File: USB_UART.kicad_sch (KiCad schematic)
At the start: 11 parts, among them J1 USB Type C Connector, U4 FT232RL

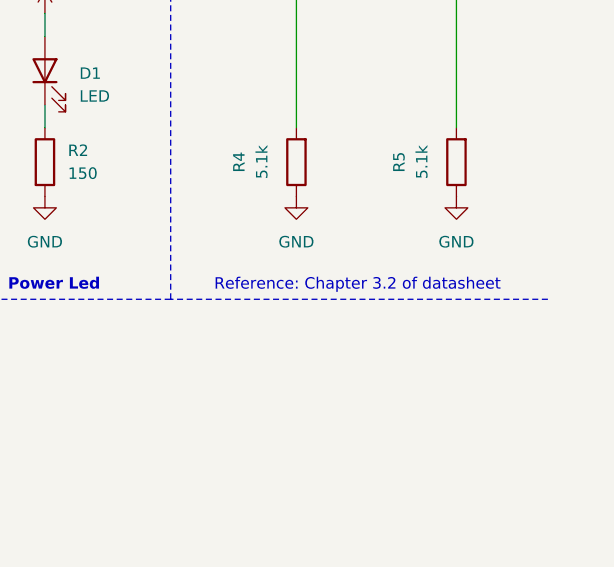
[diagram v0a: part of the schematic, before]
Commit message: fix(USB_UART): Removed an unnecessary datasheet reference
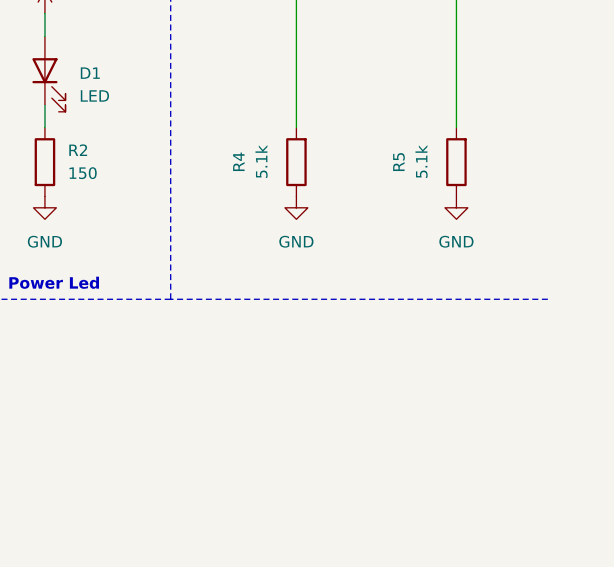
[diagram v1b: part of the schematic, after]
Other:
- note removed: "Reference: Chapter 3.2 of datasheet"
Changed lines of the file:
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@@
 	(generator_version "9.0")
 	(paper "A4")
-	(text "Reference: Chapter 3.2 of datasheet"
-		(exclude_from_sim no)
-		(at 247.396 50.546 0)
-		(effects
-			(font
-				(size 1.27 1.27)
-				(color 0 0 0 1)
-			)
-			(justify left)
-		)
-	)
 	(text "TX Led"
 		(exclude_from_sim no)

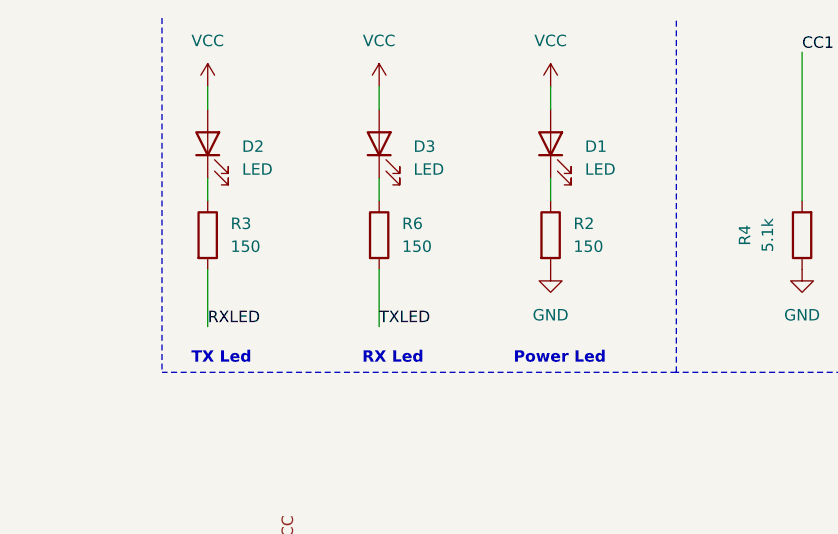
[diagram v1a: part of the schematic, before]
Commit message: fix(Power_led): Moved the power led to power tree sheet from USB UART sheet
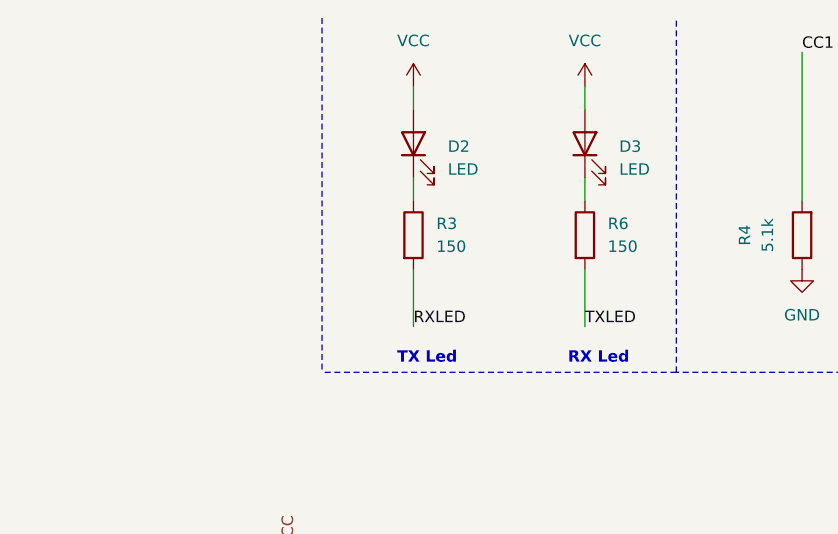
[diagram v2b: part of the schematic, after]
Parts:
- removed D1: LED, LED_SMD:LED_0603_1608Metric_Pad1.05x0.95mm_HandSolder, symbol Device:LED
- removed R2: 150, Resistor_SMD:R_0603_1608Metric_Pad0.98x0.95mm_HandSolder, symbol Device:R
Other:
- note removed: "Power Led"
- moved on the sheet: D2, D3, R3, R6

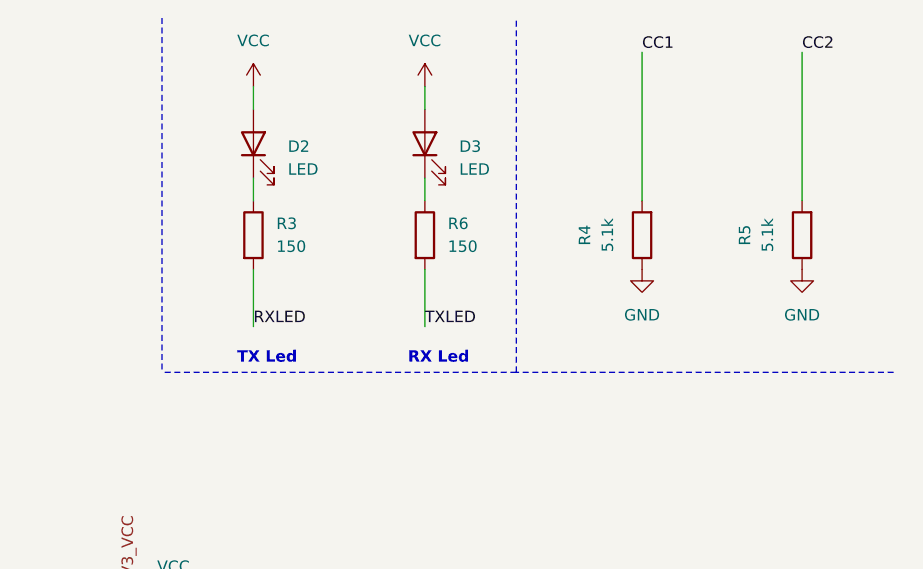
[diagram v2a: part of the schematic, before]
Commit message: feat(CC1_CC2_Resistors): Added a text to explain why the resistors of the following value is used
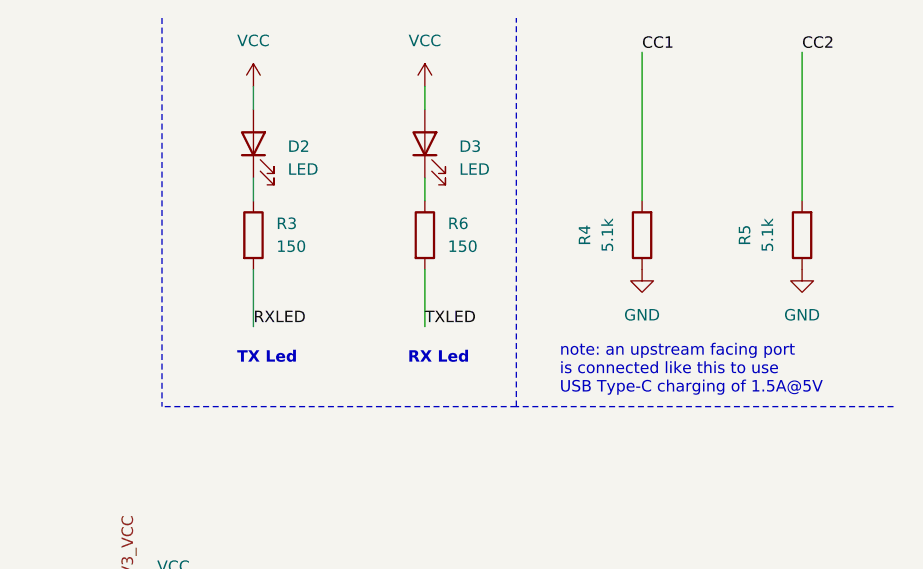
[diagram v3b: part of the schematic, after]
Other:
- note added: "note: an upstream facing port is connected like this to use USB Type-C charging of 1.5A@5V"
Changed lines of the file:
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@@
+		)
+	)
+	(text "note: an upstream facing port \nis connected like this to use \nUSB Type-C charging of 1.5A@5V"
+		(exclude_from_sim no)
+		(at 247.396 51.816 0)
+		(effects
+			(font
+				(size 1.27 1.27)
+				(thickness 0.1588)
+				(color 0 0 0 1)
+			)
+			(justify left)
 		)
 	)
@@
 	(polyline
 		(pts
-			(xy 203.2 12.7) (xy 203.2 52.07)
+			(xy 203.2 12.7) (xy 203.2 55.88)
 		)
 		(stroke
@@
 	(polyline
 		(pts
-			(xy 284.48 52.07) (xy 242.57 52.07)
+			(xy 284.48 55.88) (xy 242.57 55.88)
 		)
 		(stroke
@@
 	(polyline
 		(pts
-			(xy 242.57 52.07) (xy 203.2 52.07)
+			(xy 242.57 55.88) (xy 203.2 55.88)
 		)
 		(stroke
@@
 	(polyline
 		(pts
-			(xy 242.57 52.07) (xy 242.57 12.7)
-		)
-		(stroke
+			(xy 242.57 55.88) (xy 242.57 12.7)
+		)
+		(stroke
